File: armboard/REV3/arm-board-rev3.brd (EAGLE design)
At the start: 124.5 x 55.9 mm, 60 parts, among them J2_12V ANDERSON_POWERPOLEPP45_PCB_HO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, J2_DATA M062X3VERT, J2_GND ANDERSON_POWERPOLEPP45_PCB_HO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

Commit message: working on rev3
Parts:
- removed U$10: LTC2645, MRDT-DigitalICs:MSOP16
- added LED_12V1, LED_12V2, LED_12V3, LED_12V4: YELLOW, SparkFun-LED:LED-0603
- added RES_LEDDYNASWD1, RES_LEDDYNASWD11, RES_LEDDYNASWD3, RES_LEDDYNASWD5, RES_LEDDYNASWD7, RES_LEDDYNASWD9, RES_LEDPWR4, RES_LEDPWR5, RES_LEDPWR6, RES_LEDPWR7: 1k, SparkFun-Resistors:0603-RES
- added RES_LEDDYNASWD10, RES_LEDDYNASWD12, RES_LEDDYNASWD2, RES_LEDDYNASWD4, RES_LEDDYNASWD6, RES_LEDDYNASWD8: 2k, SparkFun-Resistors:0603-RES
- added U$9: LTC2645, MRDT-DigitalICs:MSOP16
- DYNA1: value DYNAMIXEL-1X03HORIZ -> DYNAMIXEL-1X03VERT; device MRDT-2015-Arm:MLX-SPOX5268-3PIN -> MRDT-2015-Arm:MLX-SPOX5267-3PIN
- moved DYNA1 47.6 mm to (17.8, 41.8), turned to 270 degrees
- moved RES_LEDXBRX 44.9 mm to (61.2, 37.5), flipped to the top, turned to 90 degrees
- moved LED_XB_RX 41.6 mm to (61.2, 40.8)
- moved LT1910CAP-DYNA1 41.4 mm to (41.6, 32.1)
- moved RES_LEDXBTX 41.3 mm to (59.7, 37.5), flipped to the top, turned to 90 degrees
- moved U$2 40.6 mm to (77.1, 26.9)
- moved LED_XB_TX 38.1 mm to (59.7, 40.8)
- moved FET_DYNA1 36.0 mm to (31.2, 31.6)
- moved LT1910-DYNA1 35.6 mm to (41.3, 29.1)
- moved LTC2645-CAP-IOVCC-2 19.2 mm to (81.0, 38.4)
- moved LTC2645-CAP-VCC-2 19.2 mm to (75.4, 35.3)
- moved U$11 19.2 mm to (81.4, 32.8)
- moved LED_12V 15.2 mm to (7.94, 2.41), turned to 180 degrees
- moved RES_LEDPWR2 15.2 mm to (7.94, 2.41), turned to 270 degrees
- moved LED_12VU 14.8 mm to (4.64, 2.41), turned to 180 degrees
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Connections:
- removed net ENC_EI: U$1.PD1
- removed net ENC_EO: U$1.PD0
- removed net ENC_J1: U$1.PM2
- removed net ENC_J2: U$1.PM1
- removed net ENC_WI: U$1.PM3
- removed net RC1_TO_J2: J2_DATA.P$2, U$1.PK5
- new net N$12: LED_12V2.C, RES_LEDPWR5.2
- new net N$14: LED_12V3.C, RES_LEDPWR6.2
- new net N$15: LED_12V4.C, RES_LEDPWR7.2
- new net N$7: LED_12V1.C, RES_LEDPWR4.2
- new net RC3_TO_J2: J2_DATA.P$2, U$1.PD5
- new net TX_TO_DYNA1: DYNA1.DATA, U$1.PK0, U$1.PK1
- new net TX_TO_DYNA23: DYNA2.DATA, DYNA3.DATA, U$1.PC4, U$1.PC5
- new net XB_VREF: U$2.14
- net +12V: now also LED_12V.A; no longer RES_LEDPWR2.2
- net +12V_UNREG: now also LED_12VU.A; no longer RES_LEDPWR.2
- net +3V3: now also LED_DYNASWD.A, U$9.P$12; no longer RES_LEDDYNASWD.2, U$10.P$12, U$2.14
- net +5V: now also LED_5V.A, U$9.P$1, U$9.P$13, U$9.P$7, U$9.P$9; no longer RES_LEDPWR1.2, U$10.P$1, U$10.P$13, U$10.P$7, U$10.P$9
- net ENC_EI_ANA: now also RES_LEDDYNASWD10.2, RES_LEDDYNASWD9.1
- net ENC_EI_PWM: now also RES_LEDDYNASWD9.2
- net ENC_EO_ANA: now also RES_LEDDYNASWD3.1, RES_LEDDYNASWD4.2
- net ENC_EO_PWM: now also RES_LEDDYNASWD3.2
- net ENC_J1_ANA: now also RES_LEDDYNASWD1.1, RES_LEDDYNASWD2.2, U$1.PD2, U$9.P$2; no longer U$10.P$2
- net ENC_J1_PWM: now also RES_LEDDYNASWD1.2, U$9.P$6; no longer U$10.P$6
- net ENC_J2_ANA: now also RES_LEDDYNASWD7.1, RES_LEDDYNASWD8.2, U$1.PD4, U$9.P$3; no longer U$10.P$3
- net ENC_J2_PWM: now also RES_LEDDYNASWD7.2, U$9.P$5; no longer U$10.P$5
- net ENC_WI_ANA: now also RES_LEDDYNASWD11.1, RES_LEDDYNASWD12.2
- net ENC_WI_PWM: now also RES_LEDDYNASWD11.2
- net ENC_WO_ANA: now also RES_LEDDYNASWD5.1, RES_LEDDYNASWD6.2
- net ENC_WO_PWM: now also RES_LEDDYNASWD5.2
- net GND: now also RES_LEDDYNASWD10.1, RES_LEDDYNASWD12.1, RES_LEDDYNASWD2.1, RES_LEDDYNASWD4.1, RES_LEDDYNASWD6.1, RES_LEDDYNASWD8.1, RES_LEDPWR.1, RES_LEDPWR1.1, RES_LEDPWR2.1, RES_LEDPWR4.1, RES_LEDPWR5.1, RES_LEDPWR6.1, RES_LEDPWR7.1, U$9.P$16, U$9.P$4, U$9.P$8; no longer LED_12V.C, LED_12VU.C, LED_5V.C, U$10.P$16, U$10.P$4, U$10.P$8
- net IMEAS_12V_MAIN: now also U$1.PB4; no longer U$1.PK3
- net N$3: now also LED_DYNASWD.C, RES_LEDDYNASWD.2; no longer LED_DYNASWD.A, RES_LEDDYNASWD.1
- net N$4: now also LED_12V.C, RES_LEDPWR2.2; no longer LED_12VU.A, RES_LEDPWR.1
- net N$5: now also LED_12VU.C, RES_LEDPWR.2; no longer LED_5V.A, RES_LEDPWR1.1
- net N$6: now also LED_5V.C, RES_LEDPWR1.2; no longer LED_12V.A, RES_LEDPWR2.1
- net RX_FROM_J2_TTL: now also J2_DATA.P$4; no longer J2_DATA.P$3
- net SIG_DYNA1: now also U$1.PB5; no longer U$1.PK7
- net SIG_J2: now also U$1.PM0; no longer U$1.PP4
- net SIG_MAIN: now also U$1.PK7; no longer U$1.PK2
- net SOURCE-DYNA1: now also LED_12V2.A
- net SOURCE-DYNA2: now also LED_12V3.A
- net SOURCE-DYNA3: now also LED_12V4.A
- net SOURCE-J2: now also LED_12V1.A
- net TX_TO_DYNA: now also RES_LEDDYNASWD.1; no longer DYNA1.DATA, DYNA2.DATA, DYNA3.DATA, LED_DYNASWD.C, U$1.PC4, U$1.PC5
- net TX_TO_J2_TTL: now also J2_DATA.P$3; no longer J2_DATA.P$4
- net XB_CTS: no longer U$1.PE5
- net XB_DIO0: no longer U$1.PB3
- net XB_DIO1: no longer U$1.PB2
- net XB_DIO2: no longer U$1.PM5
- net XB_DIO3: no longer U$1.PM4
- net XB_DIO4: no longer U$1.PC6
- net XB_DIO5: no longer U$1.PD3
- net XB_DTR: no longer U$1.PD4
- net XB_PWM0: no longer U$1.PB5
- net XB_PWM1: no longer U$1.PB4
- net XB_RESET: no longer U$1.PD2
- net XB_RTS: no longer U$1.PC7
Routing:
- net +12V: track 2.14 -> 109.9 mm, vias 0 -> 1
- net +3V3: track 0.00 -> 80.1 mm, vias 0 -> 2
- net TX_TO_DYNA1: track 0.00 -> 43.9 mm, vias 0 -> 2
- net IMEAS_12V_MAIN: track 0.00 -> 41.6 mm, vias 0 -> 1
- net ENC_J1_ANA: track 0.00 -> 36.7 mm, vias 0 -> 2
- net TX_TO_DYNA23: track 0.00 -> 33.9 mm
- net ENC_J2_ANA: track 0.00 -> 29.1 mm, vias 0 -> 2
- net +12V_UNREG: track 0.00 -> 27.0 mm
- net SIG_MAIN: track 0.00 -> 26.2 mm, vias 0 -> 1
- net GND: track 18.0 -> 41.0 mm, vias 5 -> 13
- net RC3_TO_J2: track 0.00 -> 21.0 mm
- net RX_FROM_XB: track 0.00 -> 19.8 mm, vias 0 -> 1
- net SIG_DYNA1: track 0.00 -> 19.4 mm, vias 0 -> 1
- net GATE-J2: track 0.00 -> 18.1 mm, vias 0 -> 2
- net GATE-MAIN: track 0.00 -> 17.4 mm, vias 0 -> 2
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- added copper zone on layer 1, net SOURCE-DYNA1
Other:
- board size 124.5 x 55.9 mm -> 124.5 x 48.3 mm
- board text added: "12V"
- board text added: "12VU"
- board text added: "5V"
- board text removed: "12V 5V 12VU"

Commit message: finished first draft, gened gerbs
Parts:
- moved U$6 50.9 mm to (48.1, 25.4)
- moved RES_LEDDYNASWD9 27.3 mm to (95.0, 44.2), turned to 90 degrees
- moved RES_LEDDYNASWD12 24.7 mm to (93.5, 44.2), flipped to the bottom, turned to 270 degrees
- moved RES_LEDDYNASWD10 23.4 mm to (95.0, 44.2), flipped to the bottom, turned to 270 degrees
- moved RES_LEDDYNASWD11 23.2 mm to (93.5, 44.2), turned to 90 degrees
- moved LTC2645-CAP-IOVCC-2 20.1 mm to (89.4, 20.1)
- moved RES_LEDDYNASWD6 19.6 mm to (91.9, 44.2), flipped to the bottom, turned to 270 degrees
- moved RES_LEDDYNASWD5 19.1 mm to (91.9, 44.2), turned to 90 degrees
- moved LTC2645-CAP-VCC-2 15.6 mm to (84.6, 22.6), turned to 90 degrees
- moved RES_LEDDYNASWD3 15.2 mm to (90.4, 44.2), turned to 90 degrees
- moved RES_LEDDYNASWD4 13.2 mm to (90.4, 44.2), flipped to the bottom, turned to 270 degrees
- moved U$11 10.4 mm to (85.2, 23.1)
- moved LT1910CAP-J2 9.43 mm to (40.3, 11.7), flipped to the bottom
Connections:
- removed net ENC_WO: U$1.PL4
- removed net SIG_SOL: U$1.PL2
- removed net TX_TO_DYNA: RES_LEDDYNASWD.1
- net ENC_EI_ANA: now also U$1.PB3, U$1.PE3, U$11.P$3; no longer U$11.P$2
- net ENC_EI_PWM: now also U$11.P$5; no longer U$11.P$6
- net ENC_EO_ANA: now also U$1.PD7, U$11.P$14; no longer U$11.P$3
- net ENC_EO_PWM: now also U$11.P$11; no longer U$11.P$5
- net ENC_WI_ANA: now also U$1.PB2, U$1.PE5, U$11.P$2; no longer U$11.P$14
- net ENC_WI_PWM: now also U$11.P$6; no longer U$11.P$11
- net ENC_WO_ANA: now also U$1.PD3
- net IMEAS_12V_EE: now also U$1.PE2; no longer U$1.PA6
- net SIG_DYNA2: now also U$1.PE1; no longer U$1.PE3
- net SIG_DYNA3: now also U$1.PF3; no longer U$1.PD7
- net TX_TO_DYNA23: now also RES_LEDDYNASWD.1
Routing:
- net +3V3: track 80.1 -> 165.3 mm, vias 2 -> 6
- net ENC_WI_ANA: track 0.00 -> 53.8 mm, vias 0 -> 4
- net ENC_EO_ANA: track 0.00 -> 53.5 mm, vias 0 -> 6
- net ENC_EI_ANA: track 0.00 -> 51.9 mm, vias 0 -> 2
- net IMEAS_12V_EE: track 0.00 -> 51.3 mm, vias 0 -> 2
- net ENC_WO_ANA: track 0.00 -> 48.3 mm, vias 0 -> 4
- net ENC_EO_PWM: track 0.00 -> 47.0 mm, vias 0 -> 4
- net ENC_WI_PWM: track 0.00 -> 41.8 mm, vias 0 -> 2
- net ENC_EI_PWM: track 0.00 -> 40.8 mm, vias 0 -> 2
- net ENC_WO_PWM: track 0.00 -> 40.8 mm, vias 0 -> 4
- net SIG_EE: track 0.00 -> 32.8 mm, vias 0 -> 2
- net GND: track 41.0 -> 54.4 mm, vias 13 -> 19
- net SIG_DYNA3: track 0.00 -> 13.1 mm
- net +12V: track 109.9 -> 97.1 mm, vias 1 -> 2
- net TX_TO_DYNA23: track 33.9 -> 43.1 mm
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
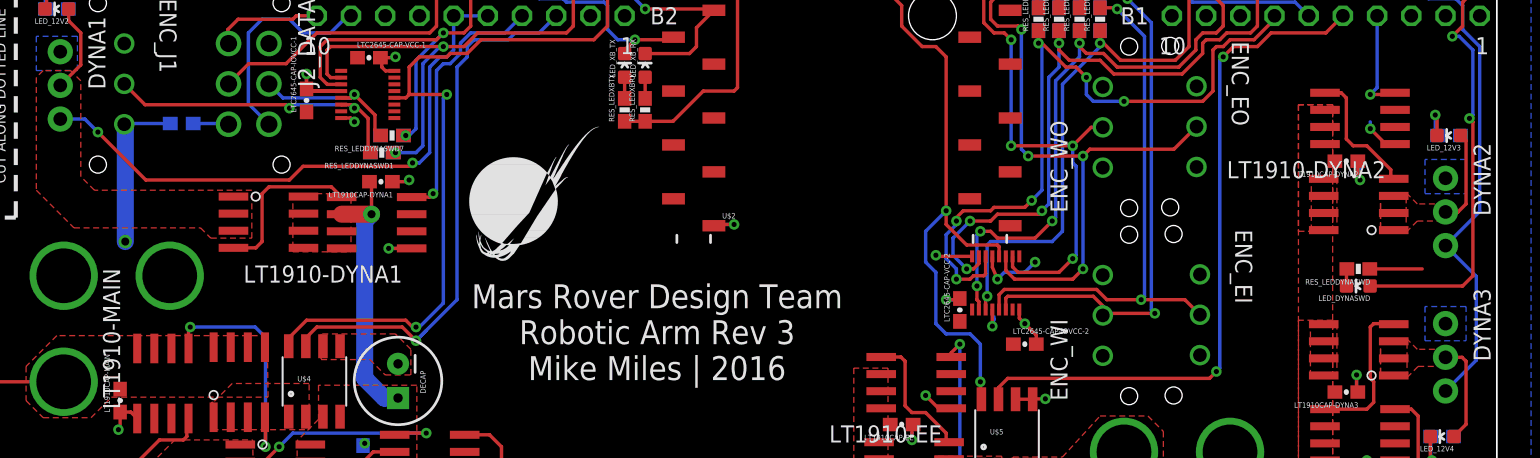
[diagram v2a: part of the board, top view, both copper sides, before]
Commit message: regened gerbers, fixed Sierra Circuits's issues regarding clearance between drill holes and copper
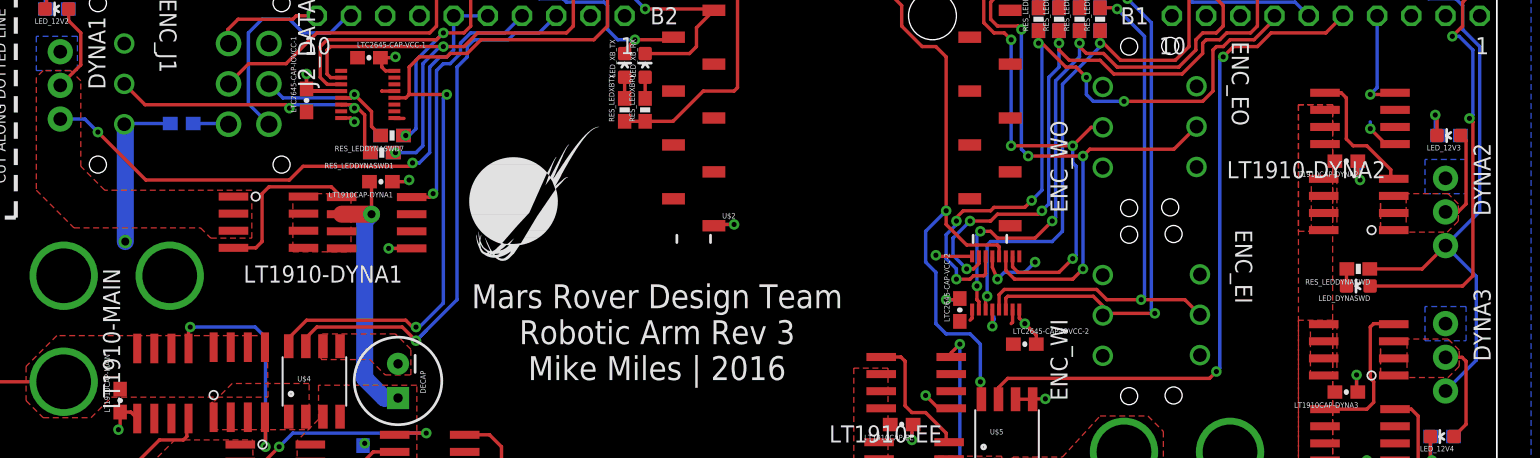
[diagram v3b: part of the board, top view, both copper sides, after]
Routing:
- net +5V: track 19.3 -> 23.0 mm
- net TX_TO_DYNA23: track 43.1 -> 45.5 mm
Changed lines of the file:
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@@
 <grid distance="0.01" unitdist="inch" unit="inch" style="lines" multiple="1" display="yes" altdistance="0.0025" altunitdist="inch" altunit="inch"/>
 <layers>
-<layer number="1" name="Top" color="4" fill="1" visible="no" active="yes"/>
-<layer number="16" name="Bottom" color="1" fill="1" visible="no" active="yes"/>
-<layer number="17" name="Pads" color="2" fill="1" visible="no" active="yes"/>
-<layer number="18" name="Vias" color="2" fill="1" visible="no" active="yes"/>
-<layer number="19" name="Unrouted" color="6" fill="1" visible="no" active="yes"/>
-<layer number="20" name="Dimension" color="5" fill="1" visible="no" active="yes"/>
+<layer number="1" name="Top" color="4" fill="1" visible="yes" active="yes"/>
+<layer number="16" name="Bottom" color="1" fill="1" visible="yes" active="yes"/>
+<layer number="17" name="Pads" color="2" fill="1" visible="yes" active="yes"/>
+<layer number="18" name="Vias" color="2" fill="1" visible="yes" active="yes"/>
+<layer number="19" name="Unrouted" color="6" fill="1" visible="yes" active="yes"/>
+<layer number="20" name="Dimension" color="5" fill="1" visible="yes" active="yes"/>
 <layer number="21" name="tPlace" color="7" fill="1" visible="yes" active="yes"/>
-<layer number="22" name="bPlace" color="7" fill="1" visible="no" active="yes"/>
-<layer number="23" name="tOrigins" color="15" fill="1" visible="no" active="yes"/>
-<layer number="24" name="bOrigins" color="15" fill="1" visible="no" active="yes"/>
+<layer number="22" name="bPlace" color="7" fill="1" visible="yes" active="yes"/>
+<layer number="23" name="tOrigins" color="15" fill="1" visible="yes" active="yes"/>
+<layer number="24" name="bOrigins" color="15" fill="1" visible="yes" active="yes"/>
 <layer number="25" name="tNames" color="7" fill="1" visible="no" active="yes"/>
 <layer number="26" name="bNames" color="7" fill="1" visible="no" active="yes"/>
@@
 <layer number="49" name="Reference" color="7" fill="1" visible="no" active="yes"/>
 <layer number="50" name="dxf" color="7" fill="1" visible="no" active="yes"/>
-<layer number="51" name="tDocu" color="7" fill="1" visible="no" active="yes"/>
-<layer number="52" name="bDocu" color="7" fill="1" visible="no" active="yes"/>
+<layer number="51" name="tDocu" color="7" fill="1" visible="yes" active="yes"/>
+<layer number="52" name="bDocu" color="7" fill="1" visible="yes" active="yes"/>
 <layer number="91" name="Nets" color="2" fill="1" visible="no" active="no"/>
 <layer number="92" name="Busses" color="1" fill="1" visible="no" active="no"/>
@@
 <contactref element="U$1" pad="GND_1" route="any" routetag="G$1.GND"/>
 <contactref element="DECAP" pad="2"/>
-<polygon width="0.254" layer="16" rank="6">
+<polygon width="0.254" layer="16" isolate="0.254" rank="6">
 <vertex x="-8.89" y="50.165"/>
 <vertex x="-8.89" y="-15.24"/>
@@
 <contactref element="U$1" pad="+5V_2" route="any" routetag="G$1.+5V"/>
 <contactref element="U$1" pad="+5V_1" route="any" routetag="G$1.+5V"/>
-<polygon width="0.254" layer="1" rank="6">
+<polygon width="0.254" layer="1" isolate="0.254" rank="6">
 <vertex x="-3.175" y="-11.43"/>
 <vertex x="130.81" y="-11.43"/>
@@
 <via x="22.606" y="27.686" extent="1-16" drill="0.6"/>
 <wire x1="22.606" y1="36.322" x2="22.5298" y2="36.3982" width="0.254" layer="16"/>
+<wire x1="85.4964" y1="22.63775" x2="85.4964" y2="21.9964" width="0.254" layer="1"/>
+<wire x1="85.4964" y1="21.9964" x2="85.344" y2="21.844" width="0.254" layer="1"/>
+<wire x1="88.498678125" y1="22.63775" x2="88.498678125" y2="21.696678125" width="0.254" layer="1"/>
+<wire x1="88.498678125" y1="21.696678125" x2="88.392" y2="21.59" width="0.254" layer="1"/>
+<wire x1="42.589446875" y1="38.8594625" x2="41.6585375" y2="38.8594625" width="0.254" layer="1"/>
+<wire x1="41.6585375" y1="38.8594625" x2="41.656" y2="38.862" width="0.254" layer="1"/>
+<wire x1="42.545" y1="36.83" x2="43.307" y2="36.83" width="0.254" layer="1"/>
+<wire x1="36.068" y1="37.3135" x2="38.63975" y2="37.358321875" width="0" layer="19" extent="1-1"/>
 </signal>
 <signal name="+3V3">
@@
 <vertex x="32.004" y="27.94"/>
 <vertex x="32.004" y="31.496"/>
-<vertex x="20.32" y="31.496"/>
-<vertex x="19.304" y="32.512"/>
+<vertex x="21.082" y="31.496"/>
+<vertex x="19.304" y="33.274"/>
 <vertex x="19.304" y="39.624"/>
 <vertex x="18.542" y="40.386"/>
@@
 <polygon width="0.3048" layer="1" thermals="no">
 <vertex x="115.824" y="28.3845"/>
-<vertex x="117.729" y="28.3845"/>
-<vertex x="118.5545" y="29.21"/>
-<vertex x="121.285" y="29.21"/>
-<vertex x="121.285" y="30.48"/>
-<vertex x="118.5545" y="30.48"/>
-<vertex x="117.7925" y="31.242"/>
+<vertex x="120.777" y="28.3845"/>
+<vertex x="121.6025" y="29.21"/>
+<vertex x="121.6025" y="30.48"/>
+<vertex x="120.8405" y="31.242"/>
 <vertex x="115.824" y="31.242"/>
 </polygon>
@@
 </polygon>
 <polygon width="0.3048" layer="1" thermals="no">
-<vertex x="117.7925" y="17.5895"/>
-<vertex x="118.618" y="18.415"/>
-<vertex x="121.285" y="18.415"/>
-<vertex x="121.285" y="19.685"/>
-<vertex x="118.5545" y="19.685"/>
-<vertex x="117.7925" y="20.447"/>
+<vertex x="120.8405" y="17.5895"/>
+<vertex x="121.666" y="18.415"/>
+<vertex x="121.666" y="19.6215"/>
+<vertex x="120.8405" y="20.447"/>
 <vertex x="115.824" y="20.447"/>
 <vertex x="115.824" y="17.5895"/>
@@
 <contactref element="RES_LEDDYNASWD1" pad="2"/>
 <wire x1="39.624" y1="37.592" x2="39.878" y2="37.592" width="0.254" layer="1"/>
-<wire x1="39.878" y1="37.592" x2="40.64" y2="36.83" width="0.254" layer="1"/>
-<wire x1="40.64" y1="36.83" x2="40.64" y2="34.456" width="0.254" layer="1"/>
-<wire x1="40.64" y1="34.456" x2="40.806" y2="34.29" width="0.254" layer="1"/>
+<wire x1="39.878" y1="37.592" x2="40.386" y2="37.084" width="0.254" layer="1"/>
+<wire x1="40.386" y1="37.084" x2="40.386" y2="34.71" width="0.254" layer="1"/>
+<wire x1="40.386" y1="34.71" x2="40.806" y2="34.29" width="0.254" layer="1"/>
 </signal>
 <signal name="ENC_J2_PWM">
@@
 <wire x1="39.36491875" y1="38.35908125" x2="38.63975" y2="38.35908125" width="0.254" layer="1"/>
 <contactref element="RES_LEDDYNASWD7" pad="2"/>
-<wire x1="39.624" y1="38.608" x2="41.148" y2="37.084" width="0.254" layer="1"/>
-<wire x1="41.148" y1="37.084" x2="41.148" y2="35.98" width="0.254" layer="1"/>
-<wire x1="41.148" y1="35.98" x2="41.568" y2="35.56" width="0.254" layer="1"/>
+<wire x1="39.624" y1="38.608" x2="40.894" y2="37.338" width="0.254" layer="1"/>
+<wire x1="40.894" y1="37.338" x2="40.894" y2="36.234" width="0.254" layer="1"/>
+<wire x1="40.894" y1="36.234" x2="41.568" y2="35.56" width="0.254" layer="1"/>
 </signal>
 <signal name="ENC_EI_PWM">
@@
 <contactref element="RES_LEDDYNASWD" pad="1"/>
 <wire x1="115.023" y1="25.654" x2="118.919" y2="25.654" width="0.254" layer="1"/>
-<wire x1="120.65" y1="27.385" x2="118.919" y2="25.654" width="0" layer="19" extent="1-1"/>
+<wire x1="118.919" y1="25.654" x2="120.65" y2="27.385" width="0.254" layer="1"/>
 </signal>
 <signal name="TX_TO_DYNA1">

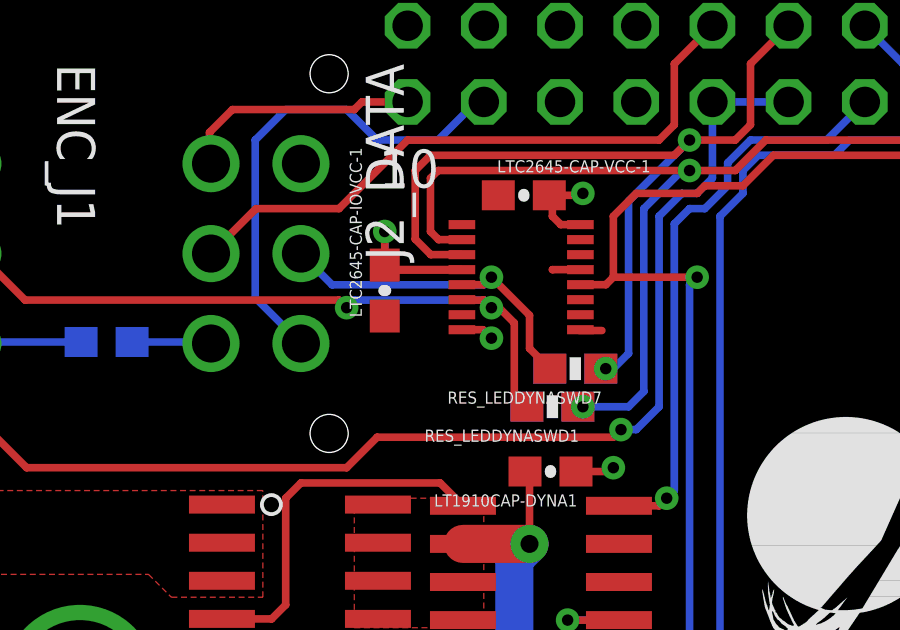
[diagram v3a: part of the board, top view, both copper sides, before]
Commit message: WARNING fixed potential issue of LTC2645 in upper left corner (U$9) not being connected to 5V - may need to fix on board when it arrives, ad
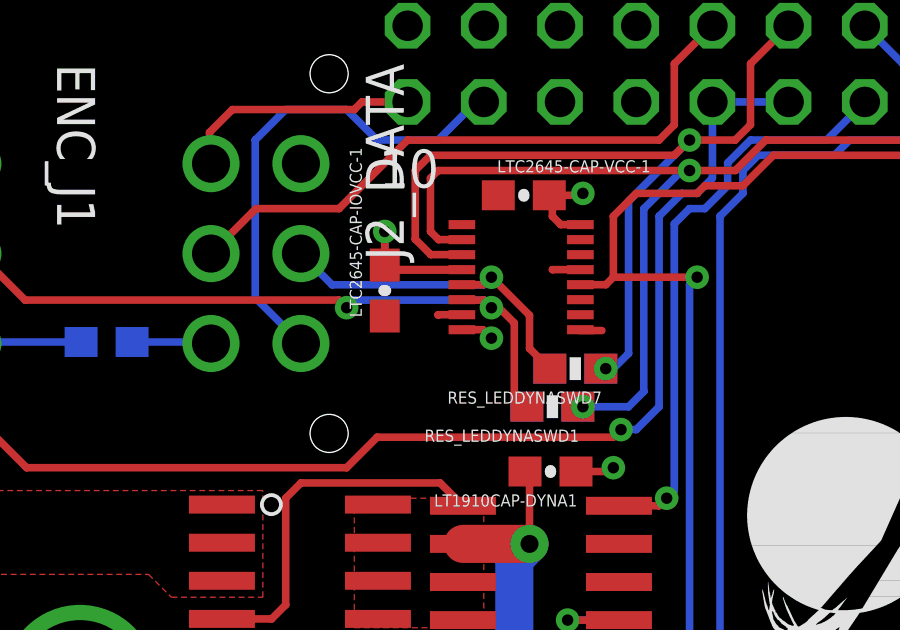
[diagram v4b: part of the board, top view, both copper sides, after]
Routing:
- net +5V: track 23.0 -> 23.8 mm
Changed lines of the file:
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@@
 <wire x1="41.6585375" y1="38.8594625" x2="41.656" y2="38.862" width="0.254" layer="1"/>
 <wire x1="42.545" y1="36.83" x2="43.307" y2="36.83" width="0.254" layer="1"/>
-<wire x1="36.068" y1="37.3135" x2="38.63975" y2="37.358321875" width="0" layer="19" extent="1-1"/>
+<wire x1="38.63975" y1="37.358321875" x2="37.846" y2="37.358321875" width="0.254" layer="1"/>
+<wire x1="37.846" y1="37.358321875" x2="37.846" y2="37.338" width="0.254" layer="1"/>
 </signal>
 <signal name="+3V3">
